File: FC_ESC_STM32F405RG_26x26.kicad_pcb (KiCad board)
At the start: 2 copper layers, 34 x 34 mm, 226 parts, among them J1 Conn_02x02_Odd_Even, J10 UART4, J11 PWM, J12 Conn_02x02_Odd_Even, J13 ALARM, J14 LED_STRIP, J15 RC, J16 MOTOR, J17 MOTOR, J18 MOTOR, J19 MOTOR, J2 ESC_PROG, J20 USB_A, J21 Conn_02x03_Odd_Even, J22 Conn_02x02_Odd_Even, J3 Debugger, J4 VOL_CUR, J5 RSSI, J6 I2C2_UART3, J7 SD CARD, J8 UART1, J9 UART6, Q1 SIZ200, Q10 SIZ200, Q11 SIZ200, Q12 SIZ200, Q2 SIZ200, Q3 SIZ200, Q4 SIZ200, Q5 SIZ200, Q6 SIZ200, Q7 SIZ200, Q8 SIZ200, Q9 SIZ200, U1 EFM8BB21, U10 FD6288Q, U11 outline, U12 MPU-6000, U13 BMP280, U14 LM358, U15 STM32F405RGTx, U16 TPS54331D, U2 EFM8BB21, U3 TPS54560BDDA, U4 FD6288Q, U5 FD6288Q, U6 AT7456, U7 EFM8BB21, U8 EFM8BB21, U9 FD6288Q, Y1 8MHz, Y2 8Mhz

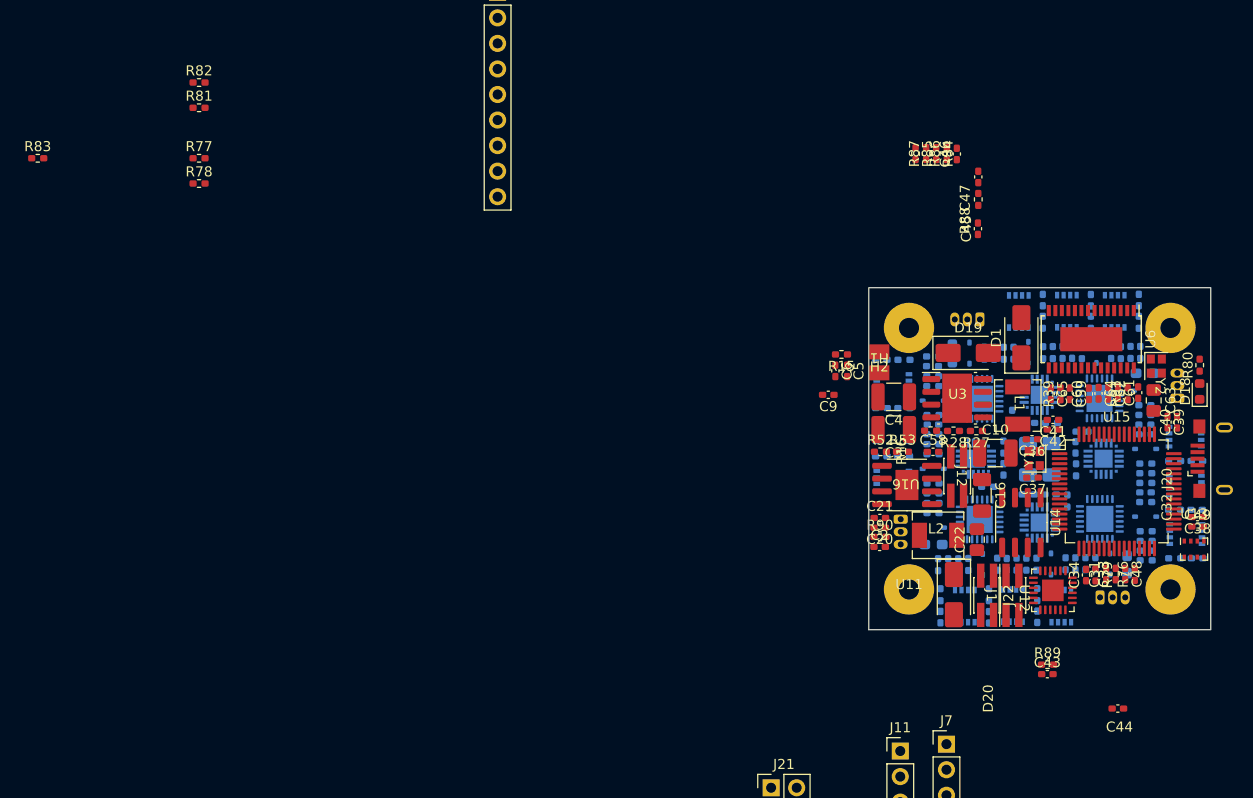
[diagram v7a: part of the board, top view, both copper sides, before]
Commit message: update placement
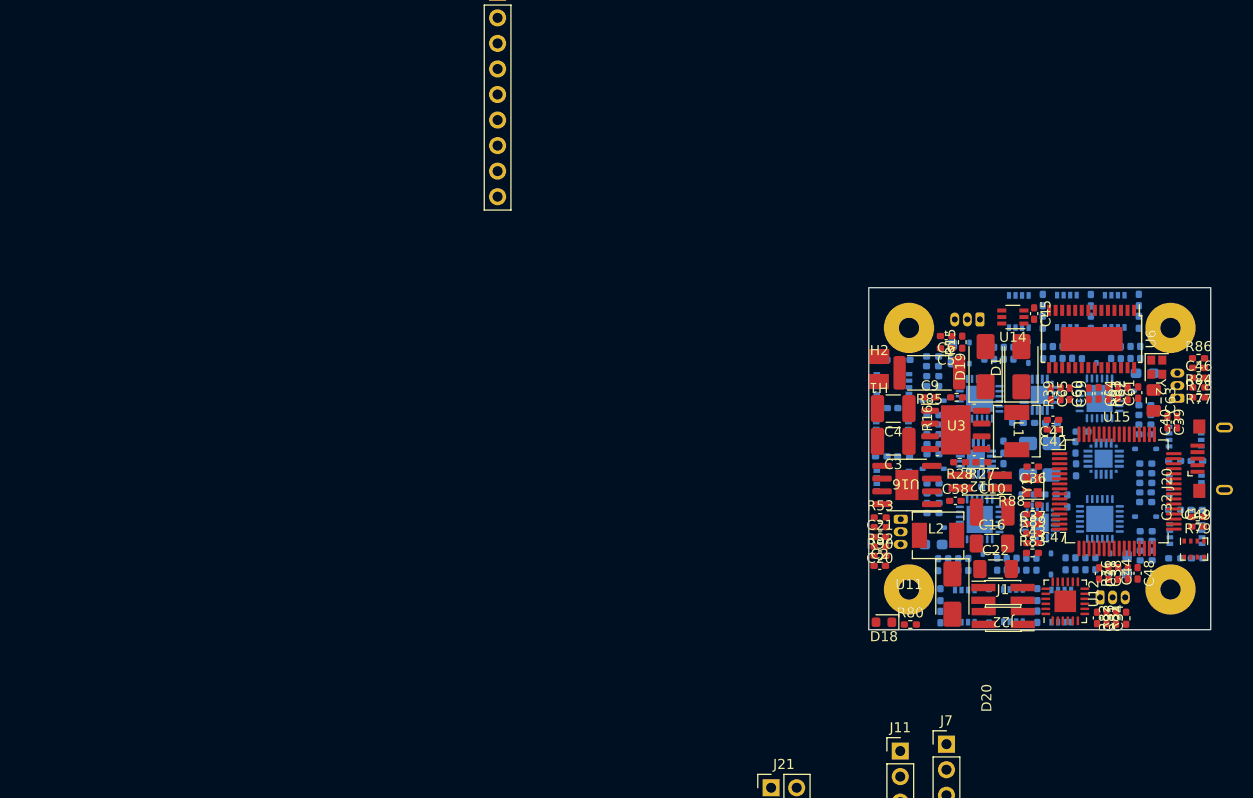
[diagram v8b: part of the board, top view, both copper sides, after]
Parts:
- removed R87: Rf_Cur, Resistor_SMD:R_0402_1005Metric_Pad0.72x0.64mm_HandSolder
- C22: footprint Capacitor_SMD:C_0805_2012Metric_Pad1.18x1.45mm_HandSolder -> Capacitor_SMD:C_1206_3216Metric_Pad1.33x1.80mm_HandSolder
- H1: value VBAT -> VBAT+
- H2: value GND -> VBAT-
- R85: footprint Resistor_SMD:R_0402_1005Metric_Pad0.72x0.64mm_HandSolder -> Resistor_SMD:R_2512_6332Metric
- U14: value LM358 -> ~; footprint Package_SO:SOIC-8_3.9x4.9mm_P1.27mm -> Package_TO_SOT_SMD:Texas_R-PDSO-G6
- moved R83 106.4 mm to (214.8, 89.6)
- moved R82 105.6 mm to (223.1, 96.1), turned to 90 degrees
- moved R81 105.2 mm to (224.1, 96.1), turned to 90 degrees
- moved R77 102.0 mm to (231.4, 73.1), turned to 180 degrees
- moved R78 101.6 mm to (231.4, 74.1)
- moved D18 38.9 mm to (200.1, 96.5), turned to 180 degrees
- moved R80 38.6 mm to (202.7, 96.7), turned to 0 degrees
- moved C47 34.9 mm to (214.9, 86.7), turned to 180 degrees
- moved R84 33.7 mm to (231.3, 71.2), turned to 180 degrees
- moved C46 32.8 mm to (231.4, 72.2), turned to 0 degrees
- moved R86 32.3 mm to (231.3, 70.3), turned to 0 degrees
- moved R88 31.8 mm to (214.9, 85.8), turned to 0 degrees
- moved R85 21.8 mm to (204.6, 71.7), turned to 180 degrees
- moved U14 20.4 mm to (212.9, 66.2), turned to 180 degrees
- moved C44 13.5 mm to (222.4, 91.6), turned to -90 degrees
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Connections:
- C1 pad 2: +5V -> GND
- C10 pad 2: +5V -> GND
- C16 pad 2: +5V -> GND
- C19 pad 2: +5V -> GND
- C2 pad 2: +5V -> GND
- C20 pad 2: +5V -> GND
- C22 pad 2: +5V -> GND
- C23 pad 2: +5V -> GND
- C24 pad 2: +5V -> GND
- C3 pad 2: +5V -> GND
- C31 pad 2: +5V -> GND
- C32 pad 2: +5V -> GND
- C33 pad 2: +5V -> GND
- C34 pad 2: +5V -> GND
- C36 pad 2: +5V -> GND
- C37 pad 2: +5V -> GND
- C38 pad 1: +5V -> GND
- C39 pad 1: +5V -> GND
- C4 pad 2: +5V -> GND
- C40 pad 2: +5V -> GND
- C41 pad 2: +5V -> GND
- C42 pad 2: +5V -> GND
- C43 pad 2: +5V -> GND
- C44 pad 2: +5V -> GND
- C45 pad 2: +5V -> GND
- C46 pad 2: +5V -> GND
- C47 pad 2: +5V -> GND
- C48 pad 2: +5V -> GND
- C49 pad 2: +5V -> GND
- C5 pad 2: +5V -> GND
- C50 pad 2: +5V -> GND
- C51 pad 2: +5V -> GND
- C52 pad 2: +5V -> GND
- C53 pad 2: +5V -> GND
- C54 pad 2: +5V -> GND
- C55 pad 2: +5V -> GND
- C56 pad 2: +5V -> GND
- C57 pad 2: +5V -> GND
- C58 pad 2: +5V -> GND
- C59 pad 2: +5V -> GND
- C6 pad 2: +5V -> GND
- C63 pad 2: +5V -> GND
- C64 pad 2: +5V -> GND
- C65 pad 2: +5V -> GND
- C7 pad 2: +5V -> GND
- C8 pad 2: +5V -> GND
- D1 pad 2: +5V -> GND
- D19 pad 2: +5V -> GND
- D20 pad 2: +5V -> GND
- H1 pad 1: V_BAT -> Net-(U14-+)
- H2 pad 1: +5V -> GND
- J10 pad 4: +5V -> GND
- J11 pad 5: +5V -> GND
- J13 pad 3: +5V -> GND
- J14 pad 3: +5V -> GND
- J15 pad 3: +5V -> GND
- J2 pad 9: +5V -> GND
- J20 pad 4: +5V -> GND
- J20 pad 5: +5V -> GND
- J21 pad 5: +5V -> GND
- J21 pad 6: +5V -> GND
- J3 pad 4: +5V -> GND
- J4 pad 4: +5V -> GND
- J5 pad 3: +5V -> GND
- J6 pad 4: +5V -> GND
- J7 pad 6: +5V -> GND
- J8 pad 4: +5V -> GND
- J9 pad 4: +5V -> GND
- Q1 pad 1: +5V -> GND
- Q10 pad 1: +5V -> GND
- Q11 pad 1: +5V -> GND
- Q12 pad 1: +5V -> GND
- Q2 pad 1: +5V -> GND
- Q3 pad 1: +5V -> GND
- Q4 pad 1: +5V -> GND
- Q5 pad 1: +5V -> GND
- Q6 pad 1: +5V -> GND
- Q7 pad 1: +5V -> GND
- Q8 pad 1: +5V -> GND
- Q9 pad 1: +5V -> GND
- R13 pad 1: +5V -> GND
- R14 pad 1: +5V -> GND
- R16 pad 2: +5V -> GND
- R25 pad 1: +5V -> GND
- R26 pad 1: +5V -> GND
- R28 pad 2: +5V -> GND
- R37 pad 1: +5V -> GND
- R38 pad 1: +5V -> GND
- R39 pad 2: +5V -> GND
- R53 pad 2: +5V -> GND
- R54 pad 1: +5V -> GND
- R55 pad 1: +5V -> GND
- R64 pad 1: +5V -> GND
- R65 pad 1: +5V -> GND
- R74 pad 1: +5V -> GND
- R75 pad 1: +5V -> GND
- R78 pad 2: +5V -> GND
- R84 pad 1: +5V -> GND
- R84 pad 2: Net-(U14A--) -> SENS_VOL
- R85 pad 1: +5V -> V_BAT
- R85 pad 2: Net-(U14B--) -> Net-(U14-+)
- R86 pad 1: Net-(U14A--) -> SENS_VOL
- R86 pad 2: SENS_VOL -> V_BAT
- R88 pad 1: Net-(R87-Pad2) -> Net-(U14-OUT)
- U1 pad 12: +5V -> GND
- U1 pad 21: +5V -> GND
- U1 pad 3: +5V -> GND
- U10 pad 6: +5V -> GND
- U12 pad 1: +5V -> GND
- U12 pad 11: +5V -> GND
- U12 pad 18: +5V -> GND
- U13 pad 1: +5V -> GND
- U13 pad 7: +5V -> GND
- U14 pad 1: SENS_VOL -> GND
- U14 pad 2: Net-(U14A--) -> GND
- U14 pad 3: VOL_IN -> 3V3_FC
- U14 pad 4: +5V -> Net-(U14-+)
- U14 pad 5: CUR_IN -> V_BAT
- U14 pad 6: Net-(U14B--) -> Net-(U14-OUT)
- U15 pad 12: +5V -> GND
- U15 pad 18: +5V -> GND
- U15 pad 63: +5V -> GND
- U16 pad 7: +5V -> GND
- U2 pad 12: +5V -> GND
- U2 pad 21: +5V -> GND
- U2 pad 3: +5V -> GND
- U3 pad 7: +5V -> GND
- U3 pad 9: +5V -> GND
- U4 pad 6: +5V -> GND
- U5 pad 6: +5V -> GND
- U6 pad 20: +5V -> GND
- U6 pad 23: +5V -> GND
- U6 pad 4: +5V -> GND
- U7 pad 12: +5V -> GND
- U7 pad 21: +5V -> GND
- U7 pad 3: +5V -> GND
- U8 pad 12: +5V -> GND
- U8 pad 21: +5V -> GND
- U8 pad 3: +5V -> GND
- U9 pad 6: +5V -> GND
